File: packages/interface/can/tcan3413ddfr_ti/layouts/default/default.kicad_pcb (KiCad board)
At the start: 2 copper layers, 6 parts

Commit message: Make package builds deterministic by wiring explicit local parts
The remaining packages now reference package-local concrete passives,
inductors, and other small parts directly instead of relying on generic
part-picker resolution. This aligns the source with the local
assets and removes the flaky live EasyEDA lookup path that was blocking
verification.

Constraint: Builds must not depend on unstable live part-picking when local package assets already exist
Constraint: Package-local parts remain the ownership boundary; no shared global part store was introduced
Rejected: Keep generic passives as the default style | repeated verification failures from upstream EasyEDA API instability
Rejected: Add ad hoc offline hacks around ato part-picking | weaker than making the package source deterministic
Confidence: high
Scope-risk: moderate
Reversibility: clean
Directive: For packages that already own generated local parts, instantiate those part modules directly and avoid generic passive declarations unless there is a strong reason not to
Tested:  passed for stm32g0b1kbu6_st, mcp2518fdt_e_sl_microchip, tcan3413ddfr_ti, raspberry_pi_hat_socket_zhouri, bq40z50rsmr_r2_4s_3a_ti, tps56637rpar_5v1_5a_ti, tps62933drlr_3v3_ti, bq25756rrvr_4s_2a_ti, tps2121ruxr_20v_4a_ti, and tps25730drefr_20v_3a_ti
Not-tested: Cross-package downstream integration beyond each package's default/example build
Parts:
- C1, C2: value 100nF ±10% -> (none)
- R1: value 10kΩ ±1% -> (none)
- R2: value 120Ω ±1% -> (none)
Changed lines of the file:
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@@
 			)
 		)
-		(property "Value" "10kΩ ±1%"
+		(property "Value" ""
 			(at 0 4)
 			(layer "F.Fab")
@@
 			(hide yes)
 		)
-		(property "Datasheet" "https://www.lcsc.com/datasheet/lcsc_datasheet_1811141608_YAGEO-RC0402FR-0710KL_C60490.pdf"
+		(property "Datasheet" "https://www.lcsc.com/datasheet/lcsc_datasheet_2304140030_YAGEO-RC0402FR-0710KL_C60490.pdf"
 			(at 0 0 0)
 			(layer "User.9")
@@
 			)
 		)
-		(property "Value" "120Ω ±1%"
+		(property "Value" ""
 			(at 0 4)
 			(layer "F.Fab")
@@
 			(hide yes)
 		)
-		(property "Datasheet" "https://www.lcsc.com/datasheet/lcsc_datasheet_1811141608_YAGEO-RC0402FR-07120RL_C114758.pdf"
+		(property "Datasheet" "https://www.lcsc.com/datasheet/lcsc_datasheet_2304140030_YAGEO-RC0402FR-07120RL_C114758.pdf"
 			(at 0 0 0)
 			(layer "User.9")
@@
 			)
 		)
-		(property "Value" "100nF ±10%"
+		(property "Value" ""
 			(at 0 4)
 			(layer "F.Fab")
@@
 			)
 		)
-		(property "Value" "100nF ±10%"
+		(property "Value" ""
 			(at 0 4)
 			(layer "F.Fab")

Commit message: Make package schematics more readable and align passive choices with repo guidance
This pass improves the human-facing quality of the package library.
Explicit local capacitor/resistor parts now carry short descriptive
comments at the point of use, the MCP2518FD package swaps its 1uF bulk
capacitor to a 0603 part to match the current sizing rule, and several
packages add better net-name overrides for exposed and important internal
signals.

Constraint: Repo guidance now prefers explicit local parts and expects readable schematic net names
Constraint: Passive sizing should follow the current MLCC package rule unless a justified exception is needed
Rejected: Keep part instances comment-free | explicit local part names are not readable enough by themselves
Rejected: Leave the MCP2518FD 1uF bulk cap in 0402 | conflicts with the current 1uF-10uF 0603 guidance
Confidence: medium
Scope-risk: moderate
Reversibility: clean
Directive: When instantiating explicit local resistor/capacitor parts, include a short readable comment with the key value/package characteristics unless the name is already obviously human-readable
Tested:  passed for stm32g0b1kbu6_st, mcp2518fdt_e_sl_microchip, tcan3413ddfr_ti, raspberry_pi_hat_socket_zhouri, bq40z50rsmr_r2_4s_3a_ti, tps56637rpar_5v1_5a_ti, tps62933drlr_3v3_ti, bq25756rrvr_4s_2a_ti, tps2121ruxr_20v_4a_ti, and tps25730drefr_20v_3a_ti
Not-tested: Complete elimination of all internal autogenerated net labels in every package; some deep internal nets may still remain tool-driven
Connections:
- net CAN_H_P renamed CANH
- net CAN_L_N renamed CANL
- net hv renamed +3.3V
- net lv renamed GND
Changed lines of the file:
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@@
 	)
 	(net 1 "STB")
-	(net 2 "CAN_H_P")
+	(net 2 "CANH")
 	(net 3 "A")
 	(net 4 "TXD")
 	(net 5 "RXD")
-	(net 6 "CAN_L_N")
-	(net 7 "hv")
-	(net 8 "lv")
+	(net 6 "CANL")
+	(net 7 "+3.3V")
+	(net 8 "GND")
 	(footprint "TEXAS_INSTRUMENTS_TCAN3413DDFR:SOT-23-8_L2.9-W1.6-P0.65-LS2.8-BR"
 		(layer "F.Cu")
@@
 			(size 1.25 0.35)
 			(layers "F.Cu" "F.Paste" "F.Mask")
-			(net 8 "lv")
+			(net 8 "GND")
 		)
 		(pad "3" smd oval
@@
 			(size 1.25 0.35)
 			(layers "F.Cu" "F.Paste" "F.Mask")
-			(net 7 "hv")
+			(net 7 "+3.3V")
 		)
 		(pad "4" smd oval
@@
 			(size 1.25 0.35)
 			(layers "F.Cu" "F.Paste" "F.Mask")
-			(net 2 "CAN_H_P")
+			(net 2 "CANH")
 		)
 		(pad "6" smd oval
@@
 			(size 1.25 0.35)
 			(layers "F.Cu" "F.Paste" "F.Mask")
-			(net 6 "CAN_L_N")
+			(net 6 "CANL")
 		)
 		(pad "5" smd oval
@@
 			(size 1.25 0.35)
 			(layers "F.Cu" "F.Paste" "F.Mask")
-			(net 7 "hv")
+			(net 7 "+3.3V")
 		)
 		(embedded_fonts no)
@@
 			(size 1 1.5)
 			(layers "F.Cu" "F.Mask")
-			(net 6 "CAN_L_N")
+			(net 6 "CANL")
 		)
 	)
@@
 			(size 0.57 0.54)
 			(layers "F.Cu" "F.Paste" "F.Mask")
-			(net 8 "lv")
+			(net 8 "GND")
 		)
 		(pad "1" smd rect
@@
 			(size 0.57 0.54)
 			(layers "F.Cu" "F.Paste" "F.Mask")
-			(net 2 "CAN_H_P")
+			(net 2 "CANH")
 		)
 		(embedded_fonts no)
@@
 			(size 0.5 0.54)
 			(layers "F.Cu" "F.Paste" "F.Mask")
-			(net 8 "lv")
+			(net 8 "GND")
 		)
 		(pad "1" smd rect
@@
 			(size 0.5 0.54)
 			(layers "F.Cu" "F.Paste" "F.Mask")
-			(net 7 "hv")
+			(net 7 "+3.3V")
 		)
 		(embedded_fonts no)
@@
 			(size 0.5 0.54)
 			(layers "F.Cu" "F.Paste" "F.Mask")
-			(net 8 "lv")
+			(net 8 "GND")
 		)
 		(pad "1" smd rect
@@
 			(size 0.5 0.54)
 			(layers "F.Cu" "F.Paste" "F.Mask")
-			(net 7 "hv")
+			(net 7 "+3.3V")
 		)
 		(embedded_fonts no)

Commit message: Finish removing net-name overrides from reusable packages
This completes the package-level override cleanup by deleting the remaining
`override_net_name` assignments from the library's reusable package modules and
rebuilding their checked-in layouts so generated net metadata matches source.
The package interfaces stay the same; only the forced net naming was removed so
these modules compose cleanly when imported into downstream designs.

Constraint: The library must stay reusable and avoid imposed internal net names leaking into consuming designs
Constraint: Each changed package must still verify with the repo's Atopile workflow after layout regeneration
Rejected: Stop after the battery frontend cleanup | leaves the same composition hazard in other packages
Rejected: Remove override lines without rebuilding layouts | would leave stale generated PCB net names checked into the repo
Confidence: high
Scope-risk: moderate
Reversibility: clean
Directive: Do not reintroduce `override_net_name` in reusable package modules unless a package is intentionally design-specific
Tested: `uv tool run --from atopile==0.15.4 ato --non-interactive build` in each affected package directory (stm32g0b1kbu6_st, mcp2518fdt_e_sl_microchip, tcan3413ddfr_ti, raspberry_pi_hat_socket_zhouri, tps56637rpar_5v1_5a_ti, tps62933drlr_3v3_ti, bq25756rrvr_4s_2a_ti, tps2121ruxr_20v_4a_ti, tps25730drefr_20v_3a_ti)
Not-tested: Downstream consumer projects that may have been depending on the old forced net names in generated layouts
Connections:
- net +3.3V renamed hv
- net CANH renamed CAN_H_P
- net CANL renamed CAN_L_N
- net GND renamed lv
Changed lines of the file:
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@@
 	)
 	(net 1 "STB")
-	(net 2 "CANH")
+	(net 2 "CAN_H_P")
 	(net 3 "A")
 	(net 4 "TXD")
 	(net 5 "RXD")
-	(net 6 "CANL")
-	(net 7 "+3.3V")
-	(net 8 "GND")
+	(net 6 "CAN_L_N")
+	(net 7 "hv")
+	(net 8 "lv")
 	(footprint "TEXAS_INSTRUMENTS_TCAN3413DDFR:SOT-23-8_L2.9-W1.6-P0.65-LS2.8-BR"
 		(layer "F.Cu")
@@
 			(size 1.25 0.35)
 			(layers "F.Cu" "F.Paste" "F.Mask")
-			(net 8 "GND")
+			(net 8 "lv")
 		)
 		(pad "3" smd oval
@@
 			(size 1.25 0.35)
 			(layers "F.Cu" "F.Paste" "F.Mask")
-			(net 7 "+3.3V")
+			(net 7 "hv")
 		)
 		(pad "4" smd oval
@@
 			(size 1.25 0.35)
 			(layers "F.Cu" "F.Paste" "F.Mask")
-			(net 2 "CANH")
+			(net 2 "CAN_H_P")
 		)
 		(pad "6" smd oval
@@
 			(size 1.25 0.35)
 			(layers "F.Cu" "F.Paste" "F.Mask")
-			(net 6 "CANL")
+			(net 6 "CAN_L_N")
 		)
 		(pad "5" smd oval
@@
 			(size 1.25 0.35)
 			(layers "F.Cu" "F.Paste" "F.Mask")
-			(net 7 "+3.3V")
+			(net 7 "hv")
 		)
 		(embedded_fonts no)
@@
 			(size 1 1.5)
 			(layers "F.Cu" "F.Mask")
-			(net 6 "CANL")
+			(net 6 "CAN_L_N")
 		)
 	)
@@
 			(size 0.57 0.54)
 			(layers "F.Cu" "F.Paste" "F.Mask")
-			(net 8 "GND")
+			(net 8 "lv")
 		)
 		(pad "1" smd rect
@@
 			(size 0.57 0.54)
 			(layers "F.Cu" "F.Paste" "F.Mask")
-			(net 2 "CANH")
+			(net 2 "CAN_H_P")
 		)
 		(embedded_fonts no)
@@
 			(size 0.5 0.54)
 			(layers "F.Cu" "F.Paste" "F.Mask")
-			(net 8 "GND")
+			(net 8 "lv")
 		)
 		(pad "1" smd rect
@@
 			(size 0.5 0.54)
 			(layers "F.Cu" "F.Paste" "F.Mask")
-			(net 7 "+3.3V")
+			(net 7 "hv")
 		)
 		(embedded_fonts no)
@@
 			(size 0.5 0.54)
 			(layers "F.Cu" "F.Paste" "F.Mask")
-			(net 8 "GND")
+			(net 8 "lv")
 		)
 		(pad "1" smd rect
@@
 			(size 0.5 0.54)
 			(layers "F.Cu" "F.Paste" "F.Mask")
-			(net 7 "+3.3V")
+			(net 7 "hv")
 		)
 		(embedded_fonts no)

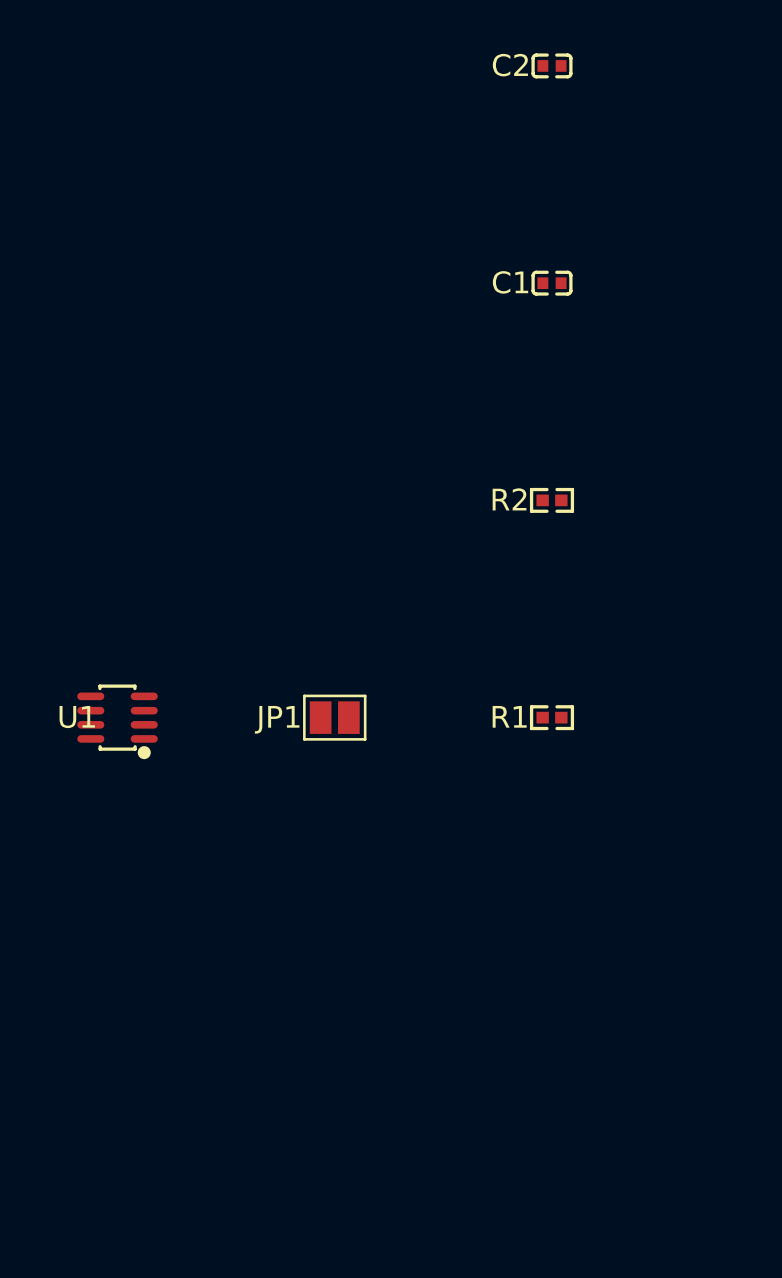
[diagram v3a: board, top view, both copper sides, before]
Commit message: TCAN3414 update
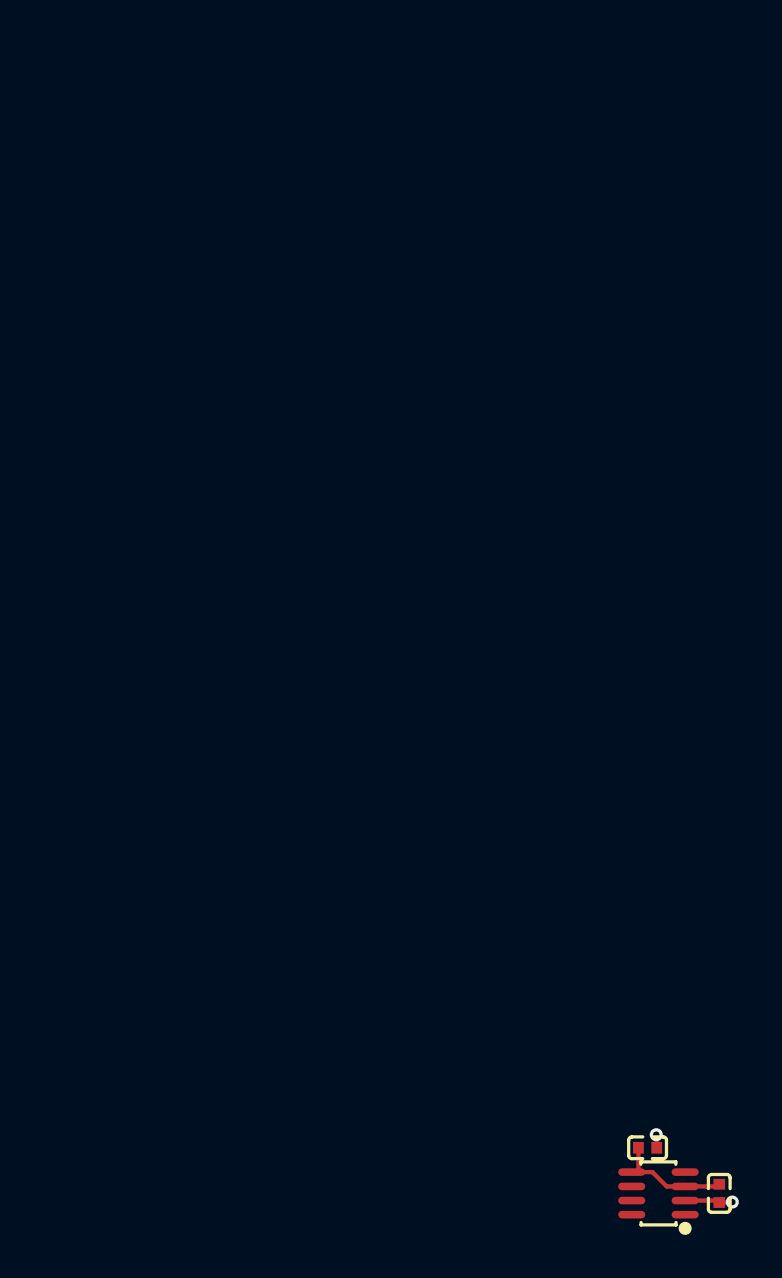
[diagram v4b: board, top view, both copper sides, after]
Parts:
- removed JP1: , SolderJumper_2_Open_P1_3mm:SolderJumper-2_P1.3mm_Open_Pad1.0x1.5mm
- removed R1: , YAGEO_RC0402FR_0710KL:R0402
- removed R2: , YAGEO_RC0402FR_07120RL:R0402
- moved C2 50.0 mm to (24.4, 19.8)
- moved C1 42.6 mm to (27.7, 21.9), turned to -90 degrees
- moved U1 33.2 mm to (24.9, 21.9)
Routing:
- net hv: track 0.00 -> 5.72 mm
- net lv: track 0.00 -> 2.82 mm, vias 0 -> 2
